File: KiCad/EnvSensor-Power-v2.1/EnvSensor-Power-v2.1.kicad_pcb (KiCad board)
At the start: 4 copper layers, 102 x 100 mm, 141 parts, among them J1 USB_B_Micro, J2 USB_C_Receptacle_USB2.0, J3 BattSense, J4 Conn_01x02, J5 Conn_01x02, J6 POWER_OUTPUT, Q1 AO6804A, Q2 IRLML2244, Q3 ZXMP6A16K, SW1 BATT_SWITCH, SW2 Start, U1 LTC3440, U2 AP9101CK, U3 MCP1825S-3.3, U4 TPS631000, U5 MCP73843-4.2, U6 MCP1826S-5.0, U7 LTC4052, U8 LM2735XMF

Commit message: Finishing touches
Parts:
- removed Q2: IRLML2244, Package_TO_SOT_SMD:SOT-23
- removed R18: 3k3, Resistor_SMD:R_0805_2012Metric
- D4: value POWER LED -> CHARGE LED (Red)
- D5: value POWER LED -> POWER LED (Red)
- J2: footprint Connector_USB:USB_C_Receptacle_HRO_TYPE-C-31-M-12 -> Connector_USB:USB_C_Receptacle_GCT_USB4135-GF-A_6P_TopMnt_Horizontal
- J4: value Conn_01x02 -> 3V3 Sense; moved to F.Cu
- J5: value Conn_01x02 -> 5V Sense; moved to F.Cu
- L2: value 100-600 -> 100-600R
- R1, R2: moved to F.Cu
- SW1: footprint Button_Switch_THT:SW_Tactile_SPST_Angled_PTS645Vx31-2LFS -> Button_Switch_THT:SW_Lever_1P2T_NKK_GW12LxH
- TP1, TP2, TP3, TP4, TP5, TP6, TS1, TS2, TS3, TS4, TS5, TS6, TS7: footprint TestPoint:TestPoint_Pad_D1.5mm -> TestPoint:TestPoint_THTPad_D1.5mm_Drill0.7mm
- U2: value AP9101CK -> AP9101CK6; footprint Package_TO_SOT_SMD:SOT-23-5 -> Package_TO_SOT_SMD:SOT-23-6
- moved R1 8.57 mm to (23.0, 50.8), turned to 180 degrees
- moved R2 8.57 mm to (23.0, 52.8), turned to 180 degrees
- moved D1 7.86 mm to (30.2, 46.0), turned to 0 degrees
- moved SW1 4.92 mm to (75.0, 28.0), turned to 180 degrees
- moved R9 3.44 mm to (25.9, 102.2), turned to 180 degrees
- moved C26 3.11 mm to (29.5, 27.2)
- moved R23 2.81 mm to (28.5, 29.2), turned to 0 degrees
- moved JP1 2.75 mm to (48.9, 24.2)
- moved R7 2.56 mm to (28.8, 102.2), turned to -90 degrees
- moved J3 2.50 mm to (50.0, 26.8)
- moved C7 2.29 mm to (28.9, 105.3)
- moved C1 1.97 mm to (24.0, 43.8)
- moved C2 1.75 mm to (63.6, 100.2)
- moved C28 1.75 mm to (56.4, 103.9)
- moved C29 1.75 mm to (59.1, 100.2)
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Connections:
- net /3V3_NOT_REG renamed /3V7_NOT_REG
- net /5V_FILTERED renamed /5V5_FILTERED
- net /5V_NOT_REG renamed /5V5_NOT_REG
- C18 pad 1: /L_CHRG_POWER -> VBUS
- Q1 pad 4: Net-(Q1-Pad4) -> /PROT_DO
- Q1 pad 6: Net-(Q1-Pad6) -> /PROT_CO
- R15 pad 2: /L_CHRG_POWER -> VBUS
- R22 pad 2: /L_CHRG_POWER -> VBUS
- R9 pad 1: Net-(R9-Pad1) -> /PROT_VM
- SW1 pad 1: /BATT_SW -> unconnected-(SW1-A-Pad1)
- U2 pad 1: Net-(R9-Pad1) -> /PROT_DO
- U2 pad 2: /PROT_VDD -> /PROT_VM
- U2 pad 3: -BATT -> /PROT_CO
- U2 pad 4: Net-(Q1-Pad4) -> unconnected-(U2-NC-Pad4)
- U2 pad 5: Net-(Q1-Pad6) -> /PROT_VDD
- U5 pad 2: /L_CHRG_POWER -> VBUS
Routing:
- net /L_CHRG_POWER: track 10.5 -> 0.00 mm
- net Net-(Q1-Pad4): track 8.65 -> 0.00 mm, vias 2 -> 0
- net +BATT: track 194.0 -> 187.1 mm, vias 2 -> 0
- net /PROT_CO: track 0.00 -> 6.70 mm
- net GND: track 160.3 -> 153.8 mm, vias 64 -> 63
- net /PROT_DO: track 0.00 -> 6.37 mm, vias 0 -> 2
- net /CHRG_CHRG: track 86.0 -> 79.7 mm, vias 4 -> 2
- net VBUS: track 232.0 -> 226.5 mm, vias 0 -> 1
- net /PROT_VM: track 0.00 -> 4.08 mm
- net /BATT_BARE: track 54.8 -> 50.7 mm
- net -BATT: track 78.3 -> 74.5 mm, vias 2 -> 0
- net Net-(Q2-Pad1): track 2.33 -> 0.00 mm
- net Net-(R9-Pad1): track 2.09 -> 0.00 mm
- net Net-(Q1-Pad6): track 1.99 -> 0.00 mm
- net +5V: track 24.1 -> 22.5 mm
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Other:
- board text added: "5V Bust Converter"
- board text added: "Batt Sense"
- board text added: "Batt prot (AP9101CK6)"
- board text added: "Dummy Load"
- board text added: "EnvSensor 2.1 - Power Supply JP, 8.04.2023"
- board text added: "LM2735XMF"
- board text added: "Power Switch"
- board text removed: "5V Bust Converter (LM2735XMF)"
- board text removed: "Batt prot (AP9101CK)"
- board text removed: "EnvSensor - Power Supply JP, 8.04.2023"

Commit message: Finishing touches
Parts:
- moved J1 9.85 mm to (22.4, 45.5)
- moved C1 7.75 mm to (24.0, 51.5)
- moved D1 7.75 mm to (30.2, 53.8)
- moved J2 7.75 mm to (23.4, 59.5)
- moved R1 7.75 mm to (23.0, 58.5)
- moved R2 7.75 mm to (23.0, 60.5)
- moved R21 7.18 mm to (27.0, 83.3)
- moved D4 7.17 mm to (25.2, 83.4)
- moved D5 7.17 mm to (25.2, 72.7)
- moved D6 7.17 mm to (23.0, 71.4)
- moved D7 7.17 mm to (23.0, 82.0)
- moved JP8 7.17 mm to (29.5, 73.7)
- moved JP9 7.17 mm to (29.5, 71.7)
- moved R19 7.17 mm to (27.0, 72.7)
- moved C41 5.24 mm to (44.0, 88.5), turned to -90 degrees
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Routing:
- net GND: track 153.8 -> 145.4 mm
- net /CHRG_ACPR: track 39.2 -> 46.4 mm
- net /CHRG_CHRG: track 79.7 -> 86.8 mm
- net +BATT: track 187.1 -> 184.0 mm
- net VBUS: track 226.5 -> 229.0 mm
- net /5V_IN: track 13.3 -> 13.9 mm
- net -BATT: vias 0 -> 1
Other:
- board text added: "3V3 Buck-Bust Converter"
- board text added: "AP9101CK6"
- board text added: "Batt Probe"
- board text added: "Batt prot"
- board text added: "LTC3440"
- board text added: "Micro USB"
- board text added: "Power input"
- board text added: "TPS631000"
- board text added: "USB C"
- board text removed: "3V3 Buck-Bust Converter (LTC3440 or TPS631000)"
- board text removed: "Batt Sense"
- board text removed: "Batt prot (AP9101CK6)"

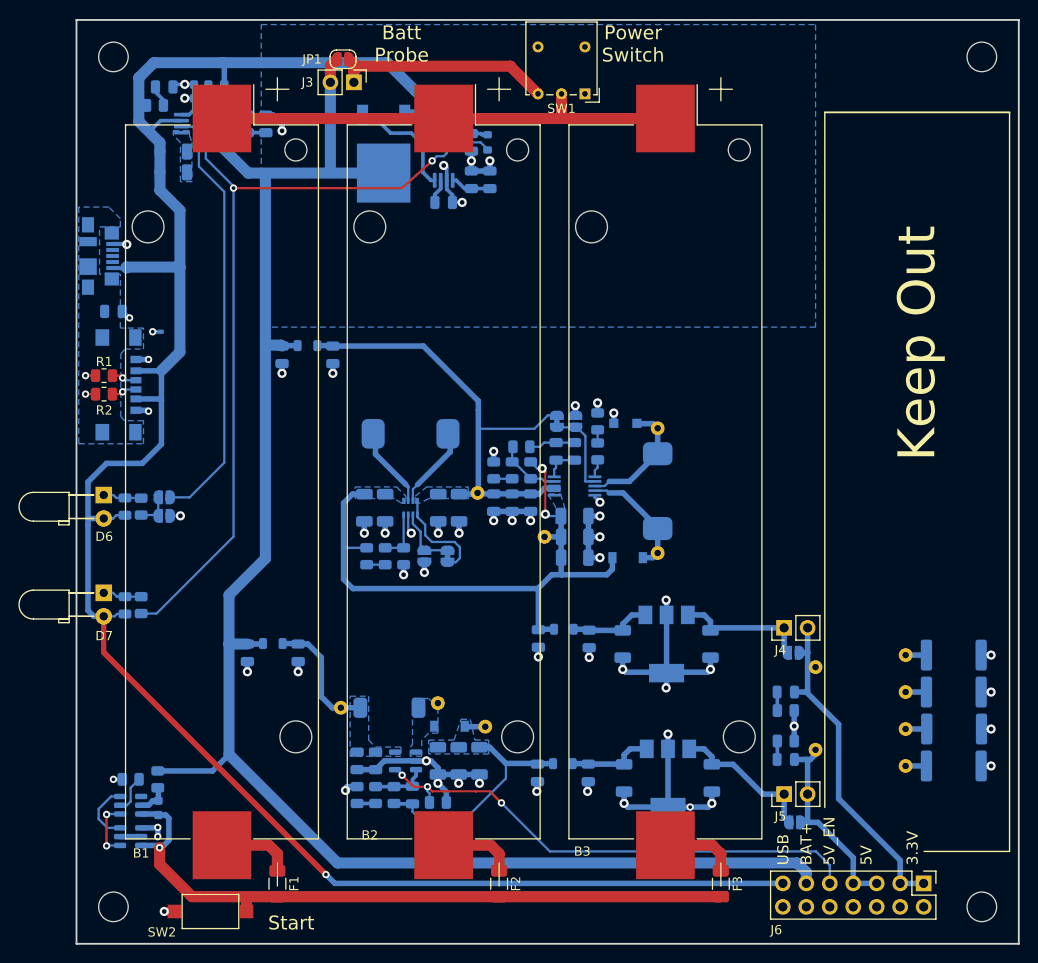
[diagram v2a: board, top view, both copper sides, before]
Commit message: LM2735 fixes
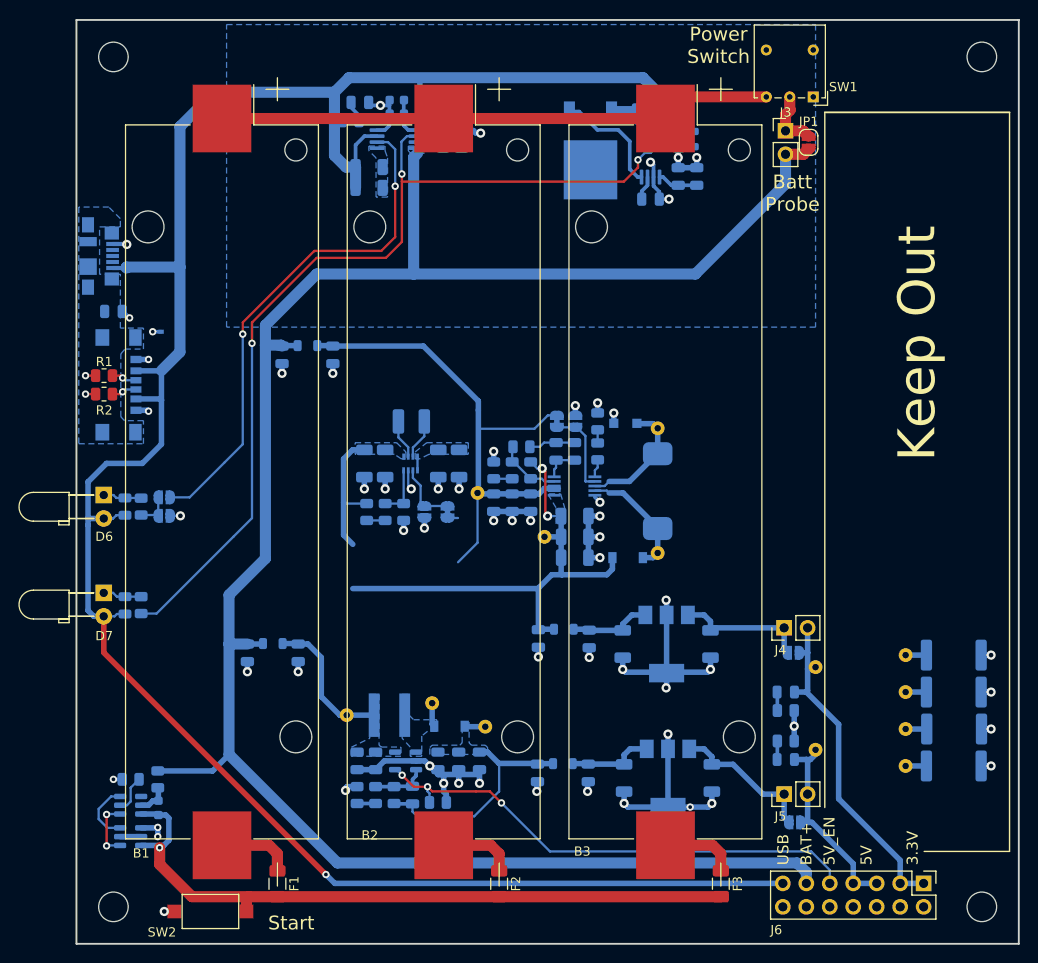
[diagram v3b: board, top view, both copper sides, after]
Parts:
- C2, C29, C30: footprint Capacitor_SMD:C_1206_3216Metric -> Capacitor_SMD:C_0805_2012Metric
- C28: value 1n8 -> 1n
- L4: footprint Inductor_SMD:L_TDK_SLF10145 -> Inductor_SMD:L_1210_3225Metric
- L5: value SLF7045T-3R3M2R5-PF / 3u3 -> MSS5131-473MLC / 47u; footprint Inductor_SMD:L_TDK_SLF7045 -> Inductor_SMD:L_Coilcraft_XAL5030-XXX
- R32: value 1M -> 300k
- U8: value LM2735XMF -> LM2735YMF
- moved JP1 51.2 mm to (99.2, 33.2), turned to -90 degrees
- moved J3 47.0 mm to (96.8, 32.0), turned to 0 degrees
- moved SW1 24.7 mm to (99.8, 28.3)
- moved C18 22.4 mm to (85.1, 32.9)
- moved C23 22.4 mm to (82.1, 39.4)
- moved C24 22.4 mm to (87.1, 36.9)
- moved C25 22.4 mm to (85.1, 36.9)
- moved Q3 22.4 mm to (75.6, 34.1)
- moved R15 22.4 mm to (82.1, 29.9)
- moved R22 22.4 mm to (86.9, 32.9)
- moved U5 22.4 mm to (82.1, 34.9)
- moved C26 21.2 mm to (50.7, 28.9)
- moved C27 21.2 mm to (59.7, 32.9)
- moved C36 21.2 mm to (61.7, 32.9)
- moved C42 21.2 mm to (54.7, 28.7)
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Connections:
- SW1 pad 2: /BATT_BARE -> /BATT_SW
- SW1 pad 3: /BATT_SW -> /BATT_BARE
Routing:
- net +BATT: track 184.0 -> 217.2 mm
- net VBUS: track 229.0 -> 253.0 mm
- net /BATT_SW: track 24.1 -> 6.64 mm
- net /CHRG_CHRG: track 86.8 -> 100.4 mm, vias 2 -> 3
- net /BATT_BARE: track 50.7 -> 59.9 mm
- net /CHRG_ACPR: track 46.4 -> 55.5 mm, vias 0 -> 2
- net /3V3_TSP_LX1: track 8.94 -> 4.32 mm
- net /3V3_TSP_LX2: track 8.73 -> 4.25 mm
- net /5V_SW: track 0.00 -> 2.59 mm
- net /BATT_3V3_FILTER: track 60.4 -> 58.5 mm
- net /5V_IN: track 13.9 -> 15.7 mm
- net GND: track 145.4 -> 144.1 mm, vias 63 -> 62
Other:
- board text added: "EnvSensor 2.1 Power Supply JP, 8.04.2023"
- board text added: "Impulse Charger"
- board text added: "LTC4052"
- board text added: "Linear Charger"
- board text added: "MCP73843-4.2"
- board text removed: "EnvSensor 2.1 - Power Supply JP, 8.04.2023"
- board text removed: "Impulse Charger (LTC4052)"
- board text removed: "Linear Charger (MCP73843-4.2)"

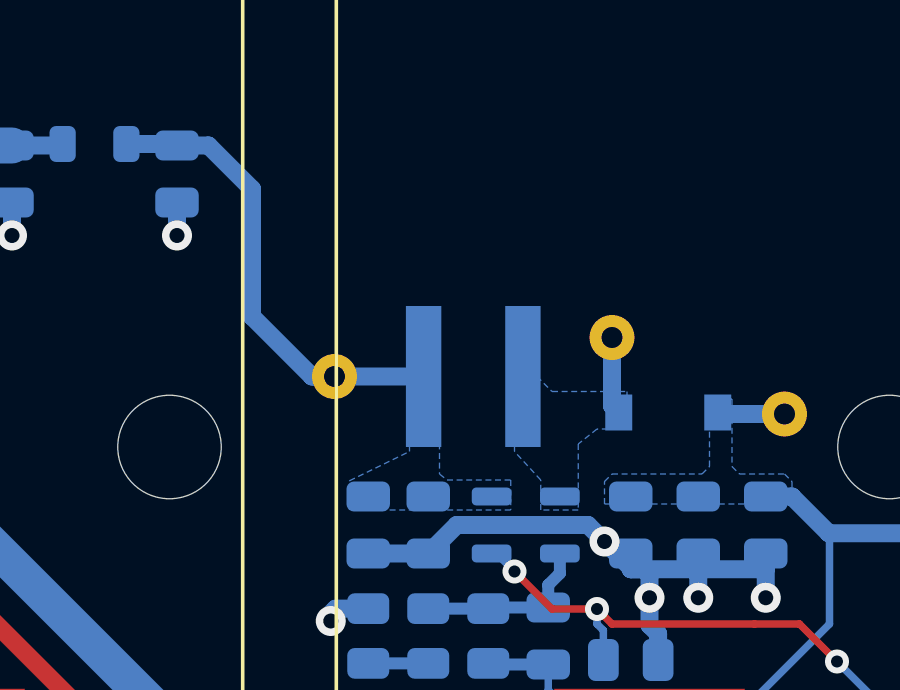
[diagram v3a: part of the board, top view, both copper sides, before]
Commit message: LM2735 fixes
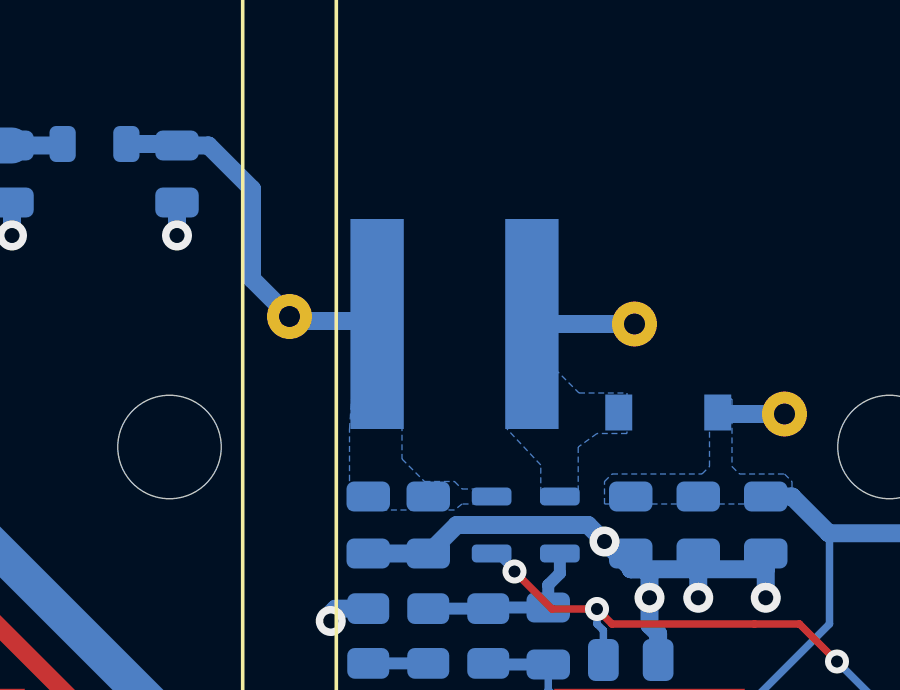
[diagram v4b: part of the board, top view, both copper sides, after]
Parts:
- L5: footprint Inductor_SMD:L_Coilcraft_XAL5030-XXX -> Inductor_SMD:L_Coilcraft_XAL8050-223
- moved TS7 2.50 mm to (47.8, 93.2)
- moved L5 1.86 mm to (53.2, 93.5)
- moved TS5 0.87 mm to (59.2, 93.5)
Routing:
- net /5V_IN: track 15.7 -> 12.7 mm
- net /5V_SW: track 2.59 -> 3.42 mm
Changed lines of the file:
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@@
   )
   (footprint "TestPoint:TestPoint_THTPad_D1.5mm_Drill0.7mm" (layer "B.Cu")
-    (at 58.5 93.95)
+    (at 59.25 93.5)
     (descr "THT pad as test Point, diameter 1.5mm, hole diameter 0.7mm")
     (tags "test point THT pad")
@@
   )
   (footprint "TestPoint:TestPoint_THTPad_D1.5mm_Drill0.7mm" (layer "B.Cu")
-    (at 49.25 95.25)
+    (at 47.75 93.25)
     (descr "THT pad as test Point, diameter 1.5mm, hole diameter 0.7mm")
     (tags "test point THT pad")
@@
     )
   )
-  (footprint "Inductor_SMD:L_Coilcraft_XAL5030-XXX" (layer "B.Cu")
-    (at 53.875 95.25)
-    (descr "Inductor, Coilcraft, XAL5030-XXX, 5.48x5.68x3.1mm, https://www.coilcraft.com/getmedia/49bc46c8-4b2c-45b9-9b6c-2eaa235ea698/xal50xx.pdf")
+  (footprint "Inductor_SMD:L_Coilcraft_XAL8050-223" (layer "B.Cu")
+    (at 53.25 93.5)
+    (descr "Inductor, Coilcraft, XAL8050-223, 8.3x8.8x5.0mm, https://www.coilcraft.com/getmedia/5885ede8-ea4f-464a-9dcb-18dbf143a845/xal8050.pdf")
     (tags "Inductor xal")
     (property "Sheetfile" "EnvSensor-Power-v2.1.kicad_sch")
@@
     (property "ki_keywords" "inductor choke coil reactor magnetic")
     (attr smd)
-    (fp_text reference "L5" (at -4.125 -2.5 180) (layer "B.SilkS")
+    (fp_text reference "L5" (at 0 5.4 180) (layer "B.SilkS")
         (effects (font (size 1 1) (thickness 0.15)) (justify mirror))
     )
-    (fp_text value "MSS5131-473MLC / 47u" (at 0 -3.84 180) (layer "B.Fab")
+    (fp_text value "MSS5131-473MLC / 47u" (at 0 -5.4 180) (layer "B.Fab")
         (effects (font (size 1 1) (thickness 0.15)) (justify mirror))
     )
     (fp_text user "${REFERENCE}" (at 0 0 180) (layer "B.Fab")
-        (effects (font (size 0.5 0.5) (thickness 0.075)) (justify mirror))
+        (effects (font (size 0.593333 0.593333) (thickness 0.089)) (justify mirror))
     )
-    (fp_line (start -3 -3.1) (end -3 -2.61)
+    (fp_line (start -4.41 -4.66) (end -4.41 -3.76)
       (stroke (width 0.12) (type solid)) (layer "B.SilkS"))
-    (fp_line (start -3 -3.1) (end 3 -3.1)
+    (fp_line (start -4.41 -4.66) (end 4.41 -4.66)
       (stroke (width 0.12) (type solid)) (layer "B.SilkS"))
-    (fp_line (start -3 3.1) (end -3 2.61)
+    (fp_line (start -4.41 4.66) (end -4.41 3.76)
       (stroke (width 0.12) (type solid)) (layer "B.SilkS"))
-    (fp_line (start -3 3.1) (end 3 3.1)
+    (fp_line (start -4.41 4.66) (end 4.41 4.66)
       (stroke (width 0.12) (type solid)) (layer "B.SilkS"))
-    (fp_line (start 3 -3.1) (end 3 -2.61)
+    (fp_line (start 4.41 -4.66) (end 4.41 -3.76)
       (stroke (width 0.12) (type solid)) (layer "B.SilkS"))
-    (fp_line (start 3 3.1) (end 3 2.61)
+    (fp_line (start 4.41 4.66) (end 4.41 3.76)
       (stroke (width 0.12) (type solid)) (layer "B.SilkS"))
-    (fp_line (start -2.99 -3.09) (end 2.99 -3.09)
+    (fp_line (start -4.4 -4.65) (end 4.4 -4.65)
       (stroke (width 0.05) (type solid)) (layer "B.CrtYd"))
-    (fp_line (start -2.99 3.09) (end -2.99 -3.09)
+    (fp_line (start -4.4 4.65) (end -4.4 -4.65)
       (stroke (width 0.05) (type solid)) (layer "B.CrtYd"))
-    (fp_line (start 2.99 -3.09) (end 2.99 3.09)
+    (fp_line (start 4.4 -4.65) (end 4.4 4.65)
       (stroke (width 0.05) (type solid)) (layer "B.CrtYd"))
-    (fp_line (start 2.99 3.09) (end -2.99 3.09)
+    (fp_line (start 4.4 4.65) (end -4.4 4.65)
       (stroke (width 0.05) (type solid)) (layer "B.CrtYd"))
-    (fp_line (start -2.74 -2.84) (end 2.74 -2.84)
+    (fp_line (start -4.15 -4.4) (end 4.15 -4.4)
       (stroke (width 0.1) (type solid)) (layer "B.Fab"))
-    (fp_line (start -2.74 2.84) (end -2.74 -2.84)
+    (fp_line (start -4.15 4.4) (end -4.15 -4.4)
       (stroke (width 0.1) (type solid)) (layer "B.Fab"))
-    (fp_line (start 2.74 -2.84) (end 2.74 2.84)
+    (fp_line (start 4.15 -4.4) (end 4.15 4.4)
       (stroke (width 0.1) (type solid)) (layer "B.Fab"))
-    (fp_line (start 2.74 2.84) (end -2.74 2.84)
+    (fp_line (start 4.15 4.4) (end -4.15 4.4)
       (stroke (width 0.1) (type solid)) (layer "B.Fab"))
-    (pad "1" smd rect (at -1.655 0) (size 1.18 4.7) (layers "B.Cu" "B.Paste" "B.Mask")
+    (pad "1" smd rect (at -2.58 0) (size 1.78 7) (layers "B.Cu" "B.Paste" "B.Mask")
       (net 45 "/5V_IN") (pinfunction "1") (pintype "passive"))
-    (pad "2" smd rect (at 1.655 0) (size 1.18 4.7) (layers "B.Cu" "B.Paste" "B.Mask")
+    (pad "2" smd rect (at 2.58 0) (size 1.78 7) (layers "B.Cu" "B.Paste" "B.Mask")
       (net 9 "/5V_SW") (pinfunction "2") (pintype "passive"))
-    (model "${KICAD7_3DMODEL_DIR}/Inductor_SMD.3dshapes/L_Coilcraft_XAL5030-XXX.wrl"
+    (model "${KICAD7_3DMODEL_DIR}/Inductor_SMD.3dshapes/L_Coilcraft_XAL8050-223.wrl"
       (offset (xyz 0 0 0))
       (scale (xyz 1 1 1))
@@
   (segment (start 47 112.5) (end 47.96 113.46) (width 0.6) (layer "B.Cu") (net 8))
   (segment (start 29.07 61.02) (end 29.2 61.15) (width 0.6) (layer "B.Cu") (net 8))
-  (segment (start 58.5 96.225) (end 58.725 96.45) (width 0.6) (layer "B.Cu") (net 9))
-  (segment (start 58.5 93.95) (end 58.5 96.225) (width 0.6) (layer "B.Cu") (net 9))
+  (segment (start 59.25 93.5) (end 55.83 93.5) (width 0.6) (layer "B.Cu") (net 9))
   (segment (start 71 73.7) (end 70.75 73.45) (width 0.25) (layer "F.Cu") (net 10))
   (segment (start 70.75 68.8875) (end 70.4125 68.55) (width 0.25) (layer "F.Cu") (net 10))
@@
   (segment (start 54.4125 102.95) (end 54.375 102.9875) (width 0.4) (layer "B.Cu") (net 44))
   (segment (start 56.7625 101.8125) (end 56.375 102.2) (width 0.4) (layer "B.Cu") (net 44))
-  (segment (start 45.05 87.55) (end 46.5 89) (width 0.6) (layer "B.Cu") (net 45))
-  (segment (start 48.5 95.25) (end 49.25 95.25) (width 0.6) (layer "B.Cu") (net 45))
-  (segment (start 46.5 89) (end 46.5 93.25) (width 0.6) (layer "B.Cu") (net 45))
   (segment (start 42.3625 87.55) (end 42.3125 87.5) (width 0.6) (layer "B.Cu") (net 45))
+  (segment (start 47.75 93.25) (end 47.899829 93.399829) (width 0.6) (layer "B.Cu") (net 45))
+  (segment (start 46.5 89) (end 46.5 92) (width 0.6) (layer "B.Cu") (net 45))
+  (segment (start 46.5 92) (end 47.75 93.25) (width 0.6) (layer "B.Cu") (net 45))
   (segment (start 44 87.55) (end 45.05 87.55) (width 0.6) (layer "B.Cu") (net 45))
+  (segment (start 45.05 87.55) (end 46.5 89) (width 0.6) (layer "B.Cu") (net 45))
   (segment (start 43.95 87.5) (end 44 87.55) (width 0.6) (layer "B.Cu") (net 45))
-  (segment (start 49.25 95.25) (end 52.22 95.25) (width 0.6) (layer "B.Cu") (net 45))
+  (segment (start 50.569829 93.399829) (end 50.67 93.5) (width 0.6) (layer "B.Cu") (net 45))
+  (segment (start 47.899829 93.399829) (end 50.569829 93.399829) (width 0.6) (layer "B.Cu") (net 45))
   (segment (start 42.3125 87.5) (end 43.95 87.5) (width 0.6) (layer "B.Cu") (net 45))
-  (segment (start 46.5 93.25) (end 48.5 95.25) (width 0.6) (layer "B.Cu") (net 45))
   (segment (start 75.0875 65.025) (end 74.1625 64.1) (width 0.25) (layer "B.Cu") (net 46))
   (segment (start 75.0875 69.925) (end 75.0875 65.025) (width 0.25) (layer "B.Cu") (net 46))
@@
     (polygon
       (pts
-        (xy 55.25 97.75)
-        (xy 55.25 93)
-        (xy 56 93)
-        (xy 56 95.25)
-        (xy 56.5 95.75)
-        (xy 59 95.75)
-        (xy 59 97)
-        (xy 58 97)
-        (xy 57.375 97.5)
-        (xy 57.375 99.7)
-        (xy 56.125 99.7)
-        (xy 56.125 98.7)
+        (xy 55 97)
+        (xy 55 92.8)
+        (xy 56.6 92.8)
+        (xy 56.6 95)
+        (xy 57.4 95.8)
+        (xy 59 95.8)
+        (xy 59 97.15)
+        (xy 58 97.15)
+        (xy 57.375 97.6)
+        (xy 57.375 99.45)
+        (xy 56.125 99.45)
+        (xy 56.125 98.2)
       )
     )
@@
     (polygon
       (pts
-        (xy 52.75 93)
-        (xy 52.75 98.5)
-        (xy 53 98.7)
-        (xy 55.125 98.7)
-        (xy 55.125 99.7)
+        (xy 51.5 93.35)
+        (xy 51.5 98)
+        (xy 52.25 98.75)
+        (xy 53.25 98.75)
+        (xy 53.5 99)
+        (xy 55 99)
+        (xy 55 99.5)
+        (xy 53.5 99.5)
+        (xy 53.25 99.7)
         (xy 49.75 99.7)
         (xy 49.75 98.725)
-        (xy 51.75 97.75)
-        (xy 51.75 93)
+        (xy 49.75 97)
+        (xy 50 93.35)
       )
     )
